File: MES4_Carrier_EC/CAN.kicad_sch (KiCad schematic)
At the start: 4 parts, among them J3 D-SUB-DR-9PCG-BB, J4 HC-RJ45-059-4-4

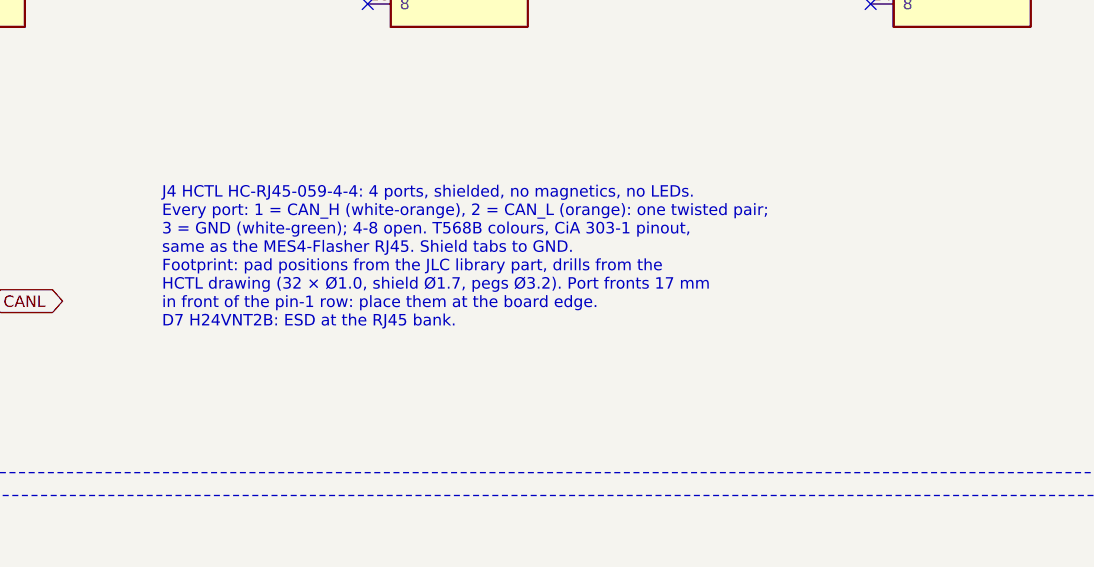
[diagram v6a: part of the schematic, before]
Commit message: Fix design review R3 findings: U9 part, stale LCSC fields, labels, J16
- B1: U9 is now YLPTEC URB2409S-6WR3 (C7468814, 9 V 6 W) on U1's
  footprint; the 10 W URB2409S-10WR3 isn't in JLC's assembly library.
  The production BOM had a 5 V module at U9 and the wrong SW2 because
  EasyEDA footprints carry an "LCSC Part" field the Fabrication Toolkit
  reads first: libs.py strips it (and the unprintable pin-1 dots it was
  copying back), and the new parts_sync.py syncs board footprints,
  values, fields and BOM flags from the schematic. TP1-TP9 and H2-H5
  are out of the BOM and CPL.
- M2 / L5: "5V LOAD CELL" across J12 / J13; "CANBUS" knockout by J4.
- B2: J16 moves 1.25 mm west so its mouth reaches the board edge.
- B8 / N6: README (one ground, U9, J16, labels, TPs), schematic notes
  and HANDOFF updated; 1:1 A4 print refreshed.
- DRC with parity at the 3 accepted J4 notes; nets, audit, DFM clean.
  production/ is stale until the Fabrication Toolkit is re-run.

Co-Authored-By: Claude Opus 5.5 <noreply@anthropic.com>
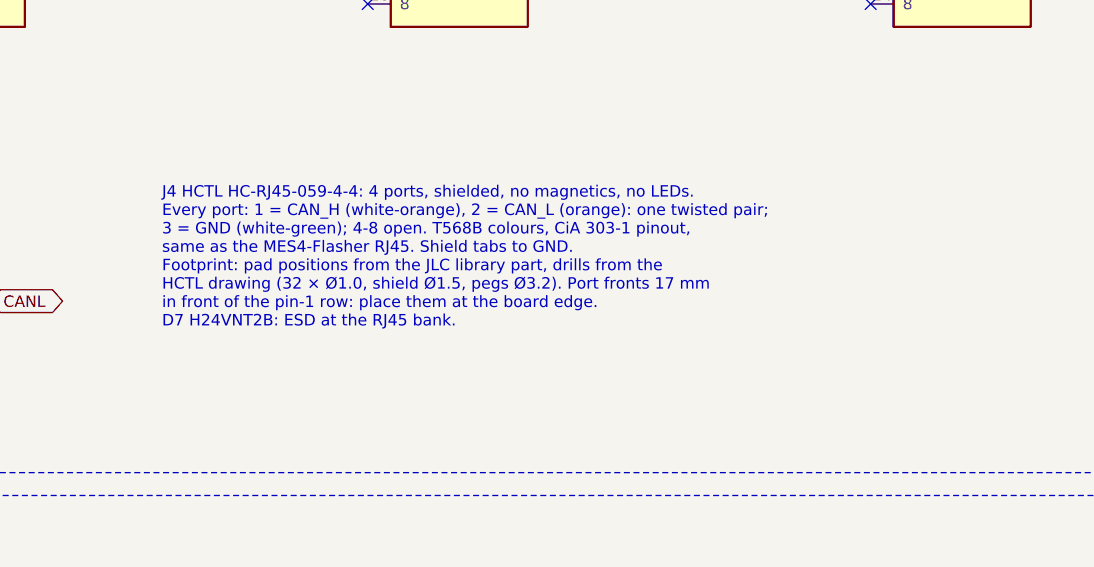
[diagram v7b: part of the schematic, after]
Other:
- note added: "J4 HCTL HC-RJ45-059-4-4: 4 ports, shielded, no magnetics, no LEDs. Every port: 1 = CAN_H (white-orange), 2 = CAN_L (orange): one twisted pair; 3 = GND (white-green); 4-8 open. T568B colours, CiA 303-1 pinout, same as the MES4-Flasher RJ45. Shield tabs to GND. Footprint: pad positions from the JLC library part, drills from the HCTL drawing (32 × Ø1.0, shield Ø1.5, pegs Ø3.2). Port fronts 17 mm in 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"
- note removed: "J4 HCTL HC-RJ45-059-4-4: 4 ports, shielded, no magnetics, no LEDs. Every port: 1 = CAN_H (white-orange), 2 = CAN_L (orange): one twisted pair; 3 = GND (white-green); 4-8 open. T568B colours, CiA 303-1 pinout, same as the MES4-Flasher RJ45. Shield tabs to GND. Footprint: pad positions from the JLC library part, drills from the HCTL drawing (32 × Ø1.0, shield Ø1.7, pegs Ø3.2). Port fronts 17 mm in 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"
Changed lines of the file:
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@@
 		)
 	)
-	(text "J4 HCTL HC-RJ45-059-4-4: 4 ports, shielded, no magnetics, no LEDs.\nEvery port: 1 = CAN_H (white-orange), 2 = CAN_L (orange): one twisted pair;\n3 = GND (white-green); 4-8 open. T568B colours, CiA 303-1 pinout,\nsame as the MES4-Flasher RJ45. Shield tabs to GND.\nFootprint: pad positions from the JLC library part, drills from the\nHCTL drawing (32 × Ø1.0, shield Ø1.7, pegs Ø3.2). Port fronts 17 mm\nin front of the pin-1 row: place them at the board edge.\nD7 H24VNT2B: ESD at the RJ45 bank."
+	(text "J4 HCTL HC-RJ45-059-4-4: 4 ports, shielded, no magnetics, no LEDs.\nEvery port: 1 = CAN_H (white-orange), 2 = CAN_L (orange): one twisted pair;\n3 = GND (white-green); 4-8 open. T568B colours, CiA 303-1 pinout,\nsame as the MES4-Flasher RJ45. Shield tabs to GND.\nFootprint: pad positions from the JLC library part, drills from the\nHCTL drawing (32 × Ø1.0, shield Ø1.5, pegs Ø3.2). Port fronts 17 mm\nin front of the pin-1 row: place them at the board edge.\nD7 H24VNT2B: ESD at the RJ45 bank."
 		(exclude_from_sim no)
 		(at 205.74 88.9 0)
